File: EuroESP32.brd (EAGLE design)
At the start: 50.8 x 86.4 mm, 127 parts, among them IC1 TL074D, IC10 MCP6004, IC2 TL072, IC3 TL072, IC4 WM8731, IC5 TL074D, IC7 ADP7118, P4 POWER_SIMPLE10, U1 LM4040SOT23, U2 MCP3204-CI/SL

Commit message: A few corrections
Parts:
- moved REGULATOR 45.8 mm to (-5.08, -22.9)
- moved U$1 45.8 mm to (11.7, -10.4)
- moved U$2 45.8 mm to (11.7, -18.0)
- moved C1 45.8 mm to (-7.62, -33.0)
- moved C6 45.8 mm to (-2.54, -33.0)
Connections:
- removed net LHPOUT: IC4.9
- removed net MICBIAS: IC4.17
- removed net MICIN: IC4.18
- removed net RHPOUT: IC4.10

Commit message: Added groups in schematic
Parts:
- removed C15, C23, C25: 10uF, parts_aman:R0805
- removed C16, C27, C29, C46: 100nF, parts_aman:RESISTOR_0603
- removed C43, C45: 1uF, parts_aman:RESISTOR_0603
- removed REGULATOR: 7805TV, linear:TO220V
- added IC6: 7805T, adafruit:TO220H
- C1, C6: device TOF:C2.5-2 -> parts_aman:R1210
- moved C6 54.5 mm to (-50.8, -58.4), turned to 0 degrees
- moved C1 46.7 mm to (-50.8, -50.8)
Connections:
- net +12V: now also IC6.1; no longer REGULATOR.1
- net +3.3VA: no longer C15.1, C16.1, C23.2, C25.2, C27.2, C29.2, C43.2, C45.2, C46.2
- net 5V: now also IC6.3; no longer REGULATOR.3
- net GND: now also IC6.2; no longer C15.2, C16.2, C23.1, C25.1, C27.1, C29.1, C43.1, C45.1, C46.1, REGULATOR.2

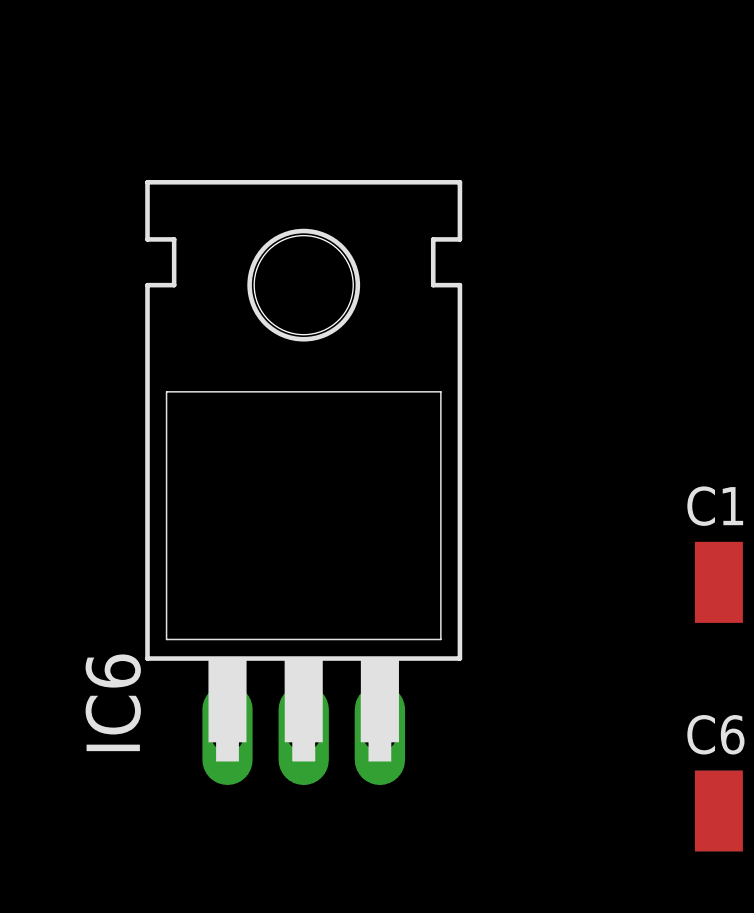
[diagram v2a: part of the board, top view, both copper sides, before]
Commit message: Changed voltage regulator
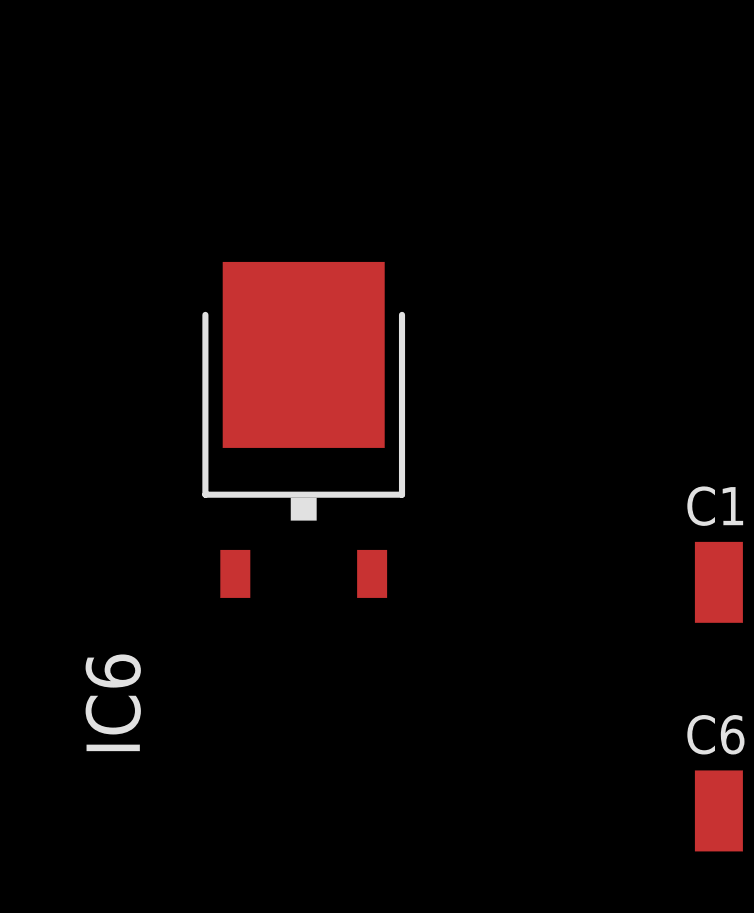
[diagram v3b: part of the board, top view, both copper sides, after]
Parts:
- IC6: value 7805T -> 7805DT; device adafruit:TO220H -> adafruit:TO252
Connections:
- net 5V: now also IC6.2; no longer IC6.3
- net GND: now also IC6.3; no longer IC6.2
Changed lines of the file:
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@@
 <attribute name="NAME" x="-53.34" y="-56.515" size="1.27" layer="25"/>
 </element>
-<element name="IC6" library="adafruit" package="TO220H" value="7805T" x="-66.04" y="-45.72" smashed="yes">
+<element name="IC6" library="adafruit" package="TO252" value="7805DT" x="-66.04" y="-45.72" smashed="yes">
 <attribute name="NAME" x="-71.501" y="-56.642" size="1.778" layer="25" ratio="10" rot="R90"/>
 <attribute name="VALUE" x="-58.674" y="-56.769" size="1.778" layer="27" ratio="10" rot="R90"/>
@@
 <contactref element="C1" pad="2"/>
 <contactref element="C6" pad="2"/>
-<contactref element="IC6" pad="2"/>
+<contactref element="IC6" pad="3"/>
 <wire x1="77.15" y1="97.79" x2="77.05" y2="99.695" width="0" layer="19" extent="16-16"/>
 <wire x1="72.3322" y1="99.65" x2="77.05" y2="99.695" width="0" layer="19" extent="16-16"/>
@@
 <wire x1="-49.4" y1="-50.8" x2="13.789" y2="-19.009" width="0" layer="19" extent="1-1"/>
 <wire x1="-49.4" y1="-58.42" x2="-49.4" y2="-50.8" width="0" layer="19" extent="1-1"/>
-<wire x1="-66.04" y1="-55.88" x2="-49.4" y2="-58.42" width="0" layer="19" extent="1-1"/>
+<wire x1="-66.04" y1="-43.22" x2="-49.4" y2="-50.8" width="0" layer="19" extent="1-1"/>
 </signal>
 <signal name="ADC_CS">
@@
 <wire x1="2.54" y1="45.72" x2="59.055" y2="47.473" width="0" layer="19" extent="16-16"/>
 <wire x1="-52.2" y1="-50.8" x2="2.54" y2="45.72" width="0" layer="19" extent="1-1"/>
-<wire x1="-68.58" y1="-55.88" x2="-52.2" y2="-50.8" width="0" layer="19" extent="1-1"/>
+<wire x1="-68.32" y1="-50.52" x2="-52.2" y2="-50.8" width="0" layer="19" extent="1-1"/>
 </signal>
 <signal name="-12V">
@@
 <contactref element="IC7" pad="3"/>
 <contactref element="C6" pad="1"/>
-<contactref element="IC6" pad="3"/>
-<wire x1="-52.2" y1="-58.42" x2="-63.5" y2="-55.88" width="0" layer="19" extent="1-1"/>
-<wire x1="-55.052" y1="36.546" x2="-63.5" y2="-55.88" width="0" layer="19" extent="1-1"/>
+<contactref element="IC6" pad="2"/>
+<wire x1="-52.2" y1="-58.42" x2="-63.76" y2="-50.52" width="0" layer="19" extent="1-1"/>
+<wire x1="-55.052" y1="36.546" x2="-63.76" y2="-50.52" width="0" layer="19" extent="1-1"/>
 <wire x1="-53.152" y1="36.546" x2="-55.052" y2="36.546" width="0" layer="19" extent="1-1"/>
 <wire x1="-53.978" y1="42.418" x2="-53.152" y2="36.546" width="0" layer="19" extent="1-1"/>

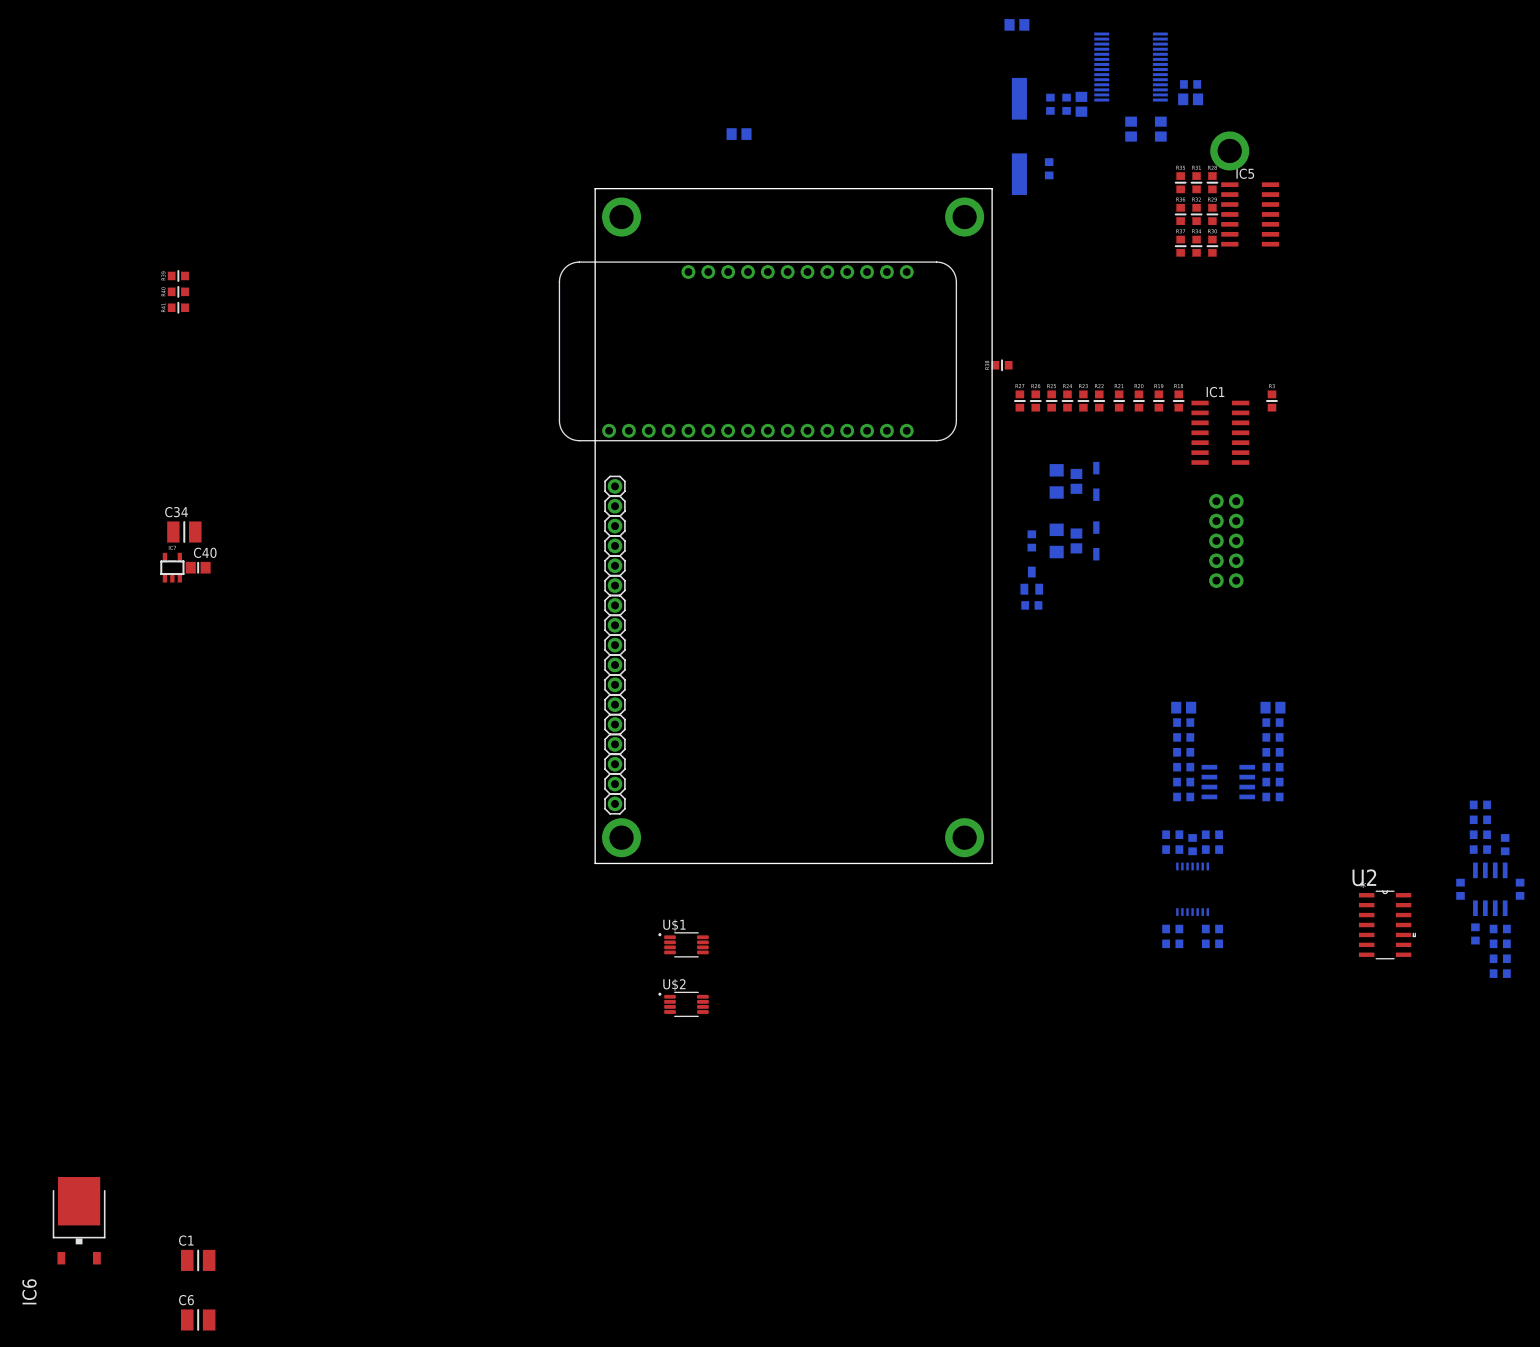
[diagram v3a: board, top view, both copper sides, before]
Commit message: Added groups and merged changes from alx-1
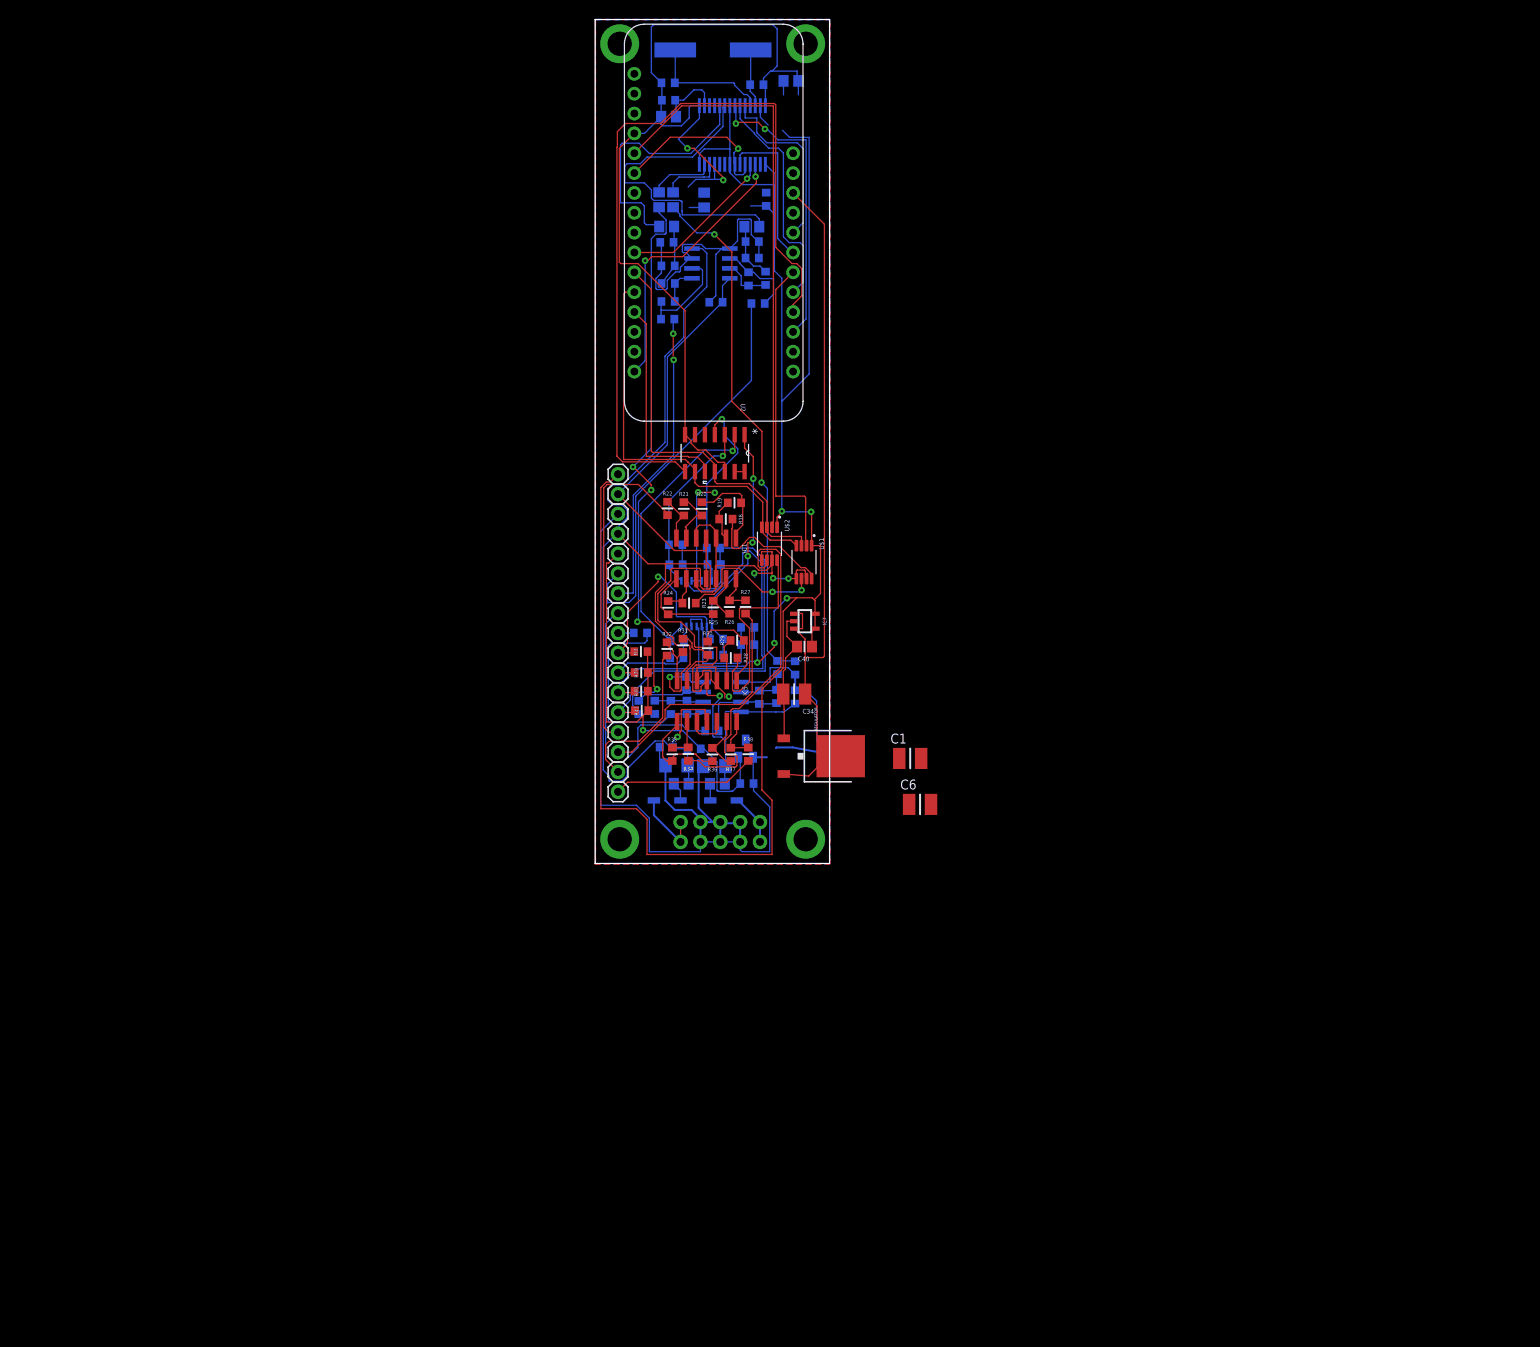
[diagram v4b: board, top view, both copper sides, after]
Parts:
- removed C30: 100nF, parts_aman:RESISTOR_0603
- removed C32: 10uF, parts_aman:R0805
- removed H2: PCB_SCREW, parts_aman:PCB_SCREW
- removed IC6: 7805DT, adafruit:TO252
- added C16: 100nF, parts_aman:RESISTOR_0603
- added C43: 1uF, parts_aman:RESISTOR_0603
- added REGULATOR: 7805DT, linear:TO252
- -10VREF: value -10VREF -> -10V
- CVIN(100K)0: value CVIN(100k)0 -> CVI0
- CVIN(100K)1: value CVIN(100K)1 -> CVI1
- CVIN(100K)2: value CVIN(100K)2 -> CVI2
- CVIN(100K)3: value CVIN(100K)3 -> CVI3
- CVOUT1: value CVOUT1 -> CVO1
- CVOUT2: value CVOUT2 -> CVO2
- CVOUT3: value CVOUT3 -> CVO3
- CVOUT4: value CVOUT4 -> CVO4
- moved C6 113.5 mm to (41.6, 7.56)
- moved C1 111.5 mm to (40.3, 13.4)
- moved R12 110.0 mm to (5.79, 29.5), turned to 0 degrees
- moved R1 108.4 mm to (5.58, 20.0), turned to 90 degrees
- moved C20 106.8 mm to (11.7, 23.0), turned to 270 degrees
- moved R6 106.6 mm to (7.63, 20.0), turned to 90 degrees
- moved R13 105.4 mm to (14.9, 17.0), turned to 0 degrees
- moved U2 104.9 mm to (15.3, 52.5), turned to 270 degrees
- moved C7 104.9 mm to (9.69, 20.0), turned to 90 degrees
- moved R10 103.2 mm to (11.7, 20.0), turned to 270 degrees
- moved H3 101.6 mm to (3.14, 104.9), turned to 270 degrees
- moved IC3 101.3 mm to (16.2, 21.3), turned to 90 degrees
- moved R7 99.7 mm to (23.3, 25.1), turned to 270 degrees
- moved R11 99.3 mm to (21.0, 21.3), turned to 270 degrees
- moved C12 99.1 mm to (9.15, 81.5), turned to 180 degrees
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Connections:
- net +12V: now also REGULATOR.1; no longer IC6.1
- net +3.3VA: now also C16.1, C43.2; no longer C30.2, C32.1
- net 5V: now also REGULATOR.2; no longer IC6.2
- net GND: now also C16.2, C43.1, REGULATOR.3; no longer C30.1, C32.2, IC6.3
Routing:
- net GND: track 0.00 -> 439.4 mm, vias 0 -> 8
- net +3.3VA: track 0.00 -> 277.6 mm, vias 0 -> 5
- net -12V: track 0.00 -> 149.2 mm, vias 0 -> 2
- net +12V: track 0.00 -> 120.7 mm, vias 0 -> 1
- net ADC_CS: track 0.00 -> 101.6 mm
- net 5V: track 0.00 -> 91.1 mm
- net N$49: track 0.00 -> 76.5 mm, vias 0 -> 4
- net DAC34_CS: track 0.00 -> 74.3 mm
- net N$57: track 0.00 -> 67.2 mm, vias 0 -> 2
- net -10VREF: track 0.00 -> 59.4 mm, vias 0 -> 1
- net N$15: track 0.00 -> 54.7 mm
- net SPI_MOSI: track 0.00 -> 52.8 mm
- net SPI_CLK: track 0.00 -> 52.3 mm
- net N$21: track 0.00 -> 51.9 mm
- net N$1: track 0.00 -> 51.8 mm
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- added copper zone on layer 1, net GND
- added copper zone on layer 16, net GND
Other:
- board size 50.8 x 86.4 mm -> 30 x 108 mm

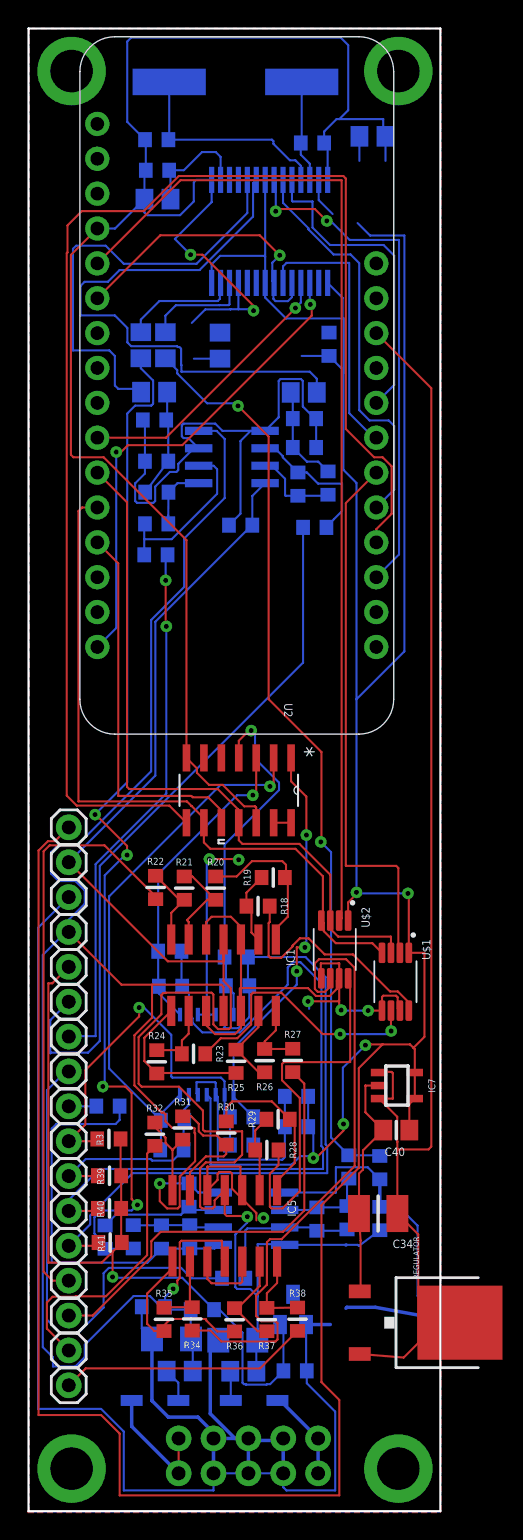
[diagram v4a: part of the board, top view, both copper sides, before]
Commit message: Moved connecters to the side
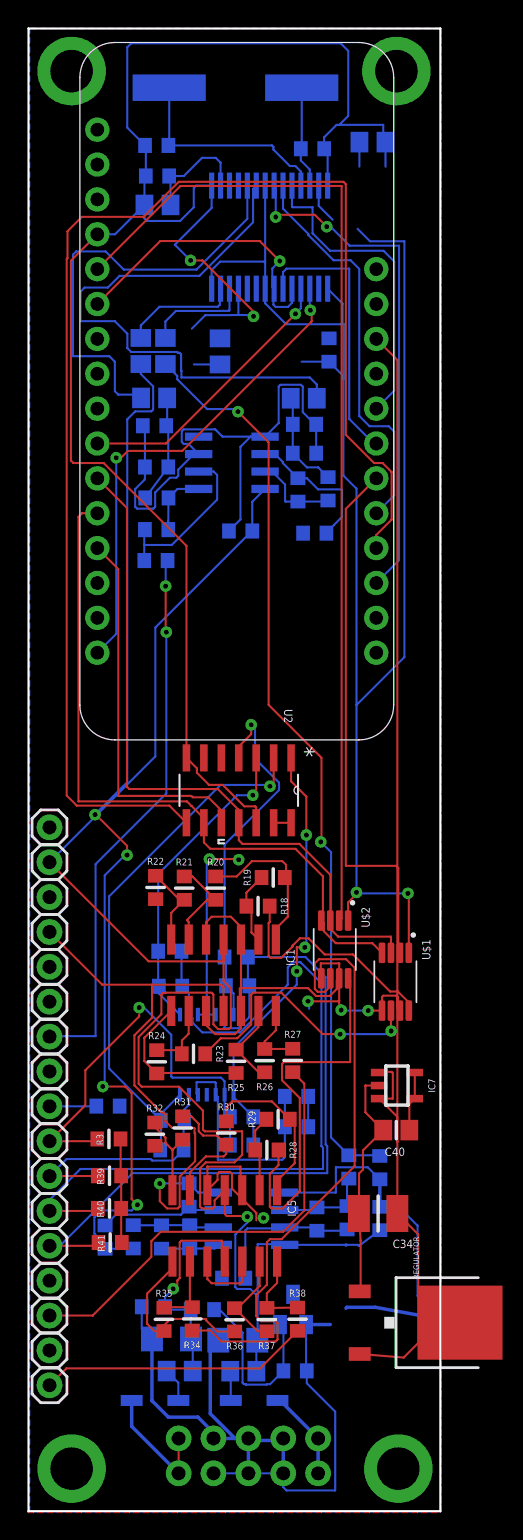
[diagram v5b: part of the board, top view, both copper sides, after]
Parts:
- moved +12V 1.40 mm to (1.53, 47.3), turned to 180 degrees
- moved +3.3VA 1.40 mm to (1.53, 49.8), turned to 180 degrees
- moved -10VREF 1.40 mm to (1.53, 39.6), turned to 180 degrees
- moved -12V 1.40 mm to (1.53, 42.2), turned to 180 degrees
- moved CVIN(100K)0 1.40 mm to (1.53, 26.9), turned to 180 degrees
- moved CVIN(100K)1 1.40 mm to (1.53, 24.4), turned to 180 degrees
- moved CVIN(100K)2 1.40 mm to (1.53, 21.9), turned to 180 degrees
- moved CVIN(100K)3 1.40 mm to (1.53, 19.3), turned to 180 degrees
- moved CVOUT1 1.40 mm to (1.53, 16.8), turned to 180 degrees
- moved CVOUT2 1.40 mm to (1.53, 14.2), turned to 180 degrees
- moved CVOUT3 1.40 mm to (1.53, 11.7), turned to 180 degrees
- moved CVOUT4 1.40 mm to (1.53, 9.17), turned to 180 degrees
- moved GND 1.40 mm to (1.53, 44.7), turned to 180 degrees
- moved J_LIN 1.40 mm to (1.53, 37.1), turned to 180 degrees
- moved J_LOUT 1.40 mm to (1.53, 32.0), turned to 180 degrees
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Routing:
- net +3.3VA: track 277.6 -> 131.6 mm, vias 5 -> 2
- net -12V: track 149.2 -> 60.2 mm
- net GND: track 439.4 -> 378.9 mm
- net N$1: track 51.8 -> 0.00 mm
- net N$25: track 42.8 -> 0.00 mm
- net -10VREF: track 59.4 -> 20.9 mm, vias 1 -> 0
- net N$2: track 35.8 -> 0.00 mm
- net N$46: track 28.7 -> 4.25 mm
- net N$29: track 21.1 -> 0.00 mm
- net 5V: track 91.1 -> 86.7 mm
- net N$15: track 54.7 -> 57.5 mm
- net N$19: track 15.6 -> 18.4 mm
- net N$21: track 51.9 -> 54.3 mm
- net N$17: track 29.0 -> 31.0 mm
- net +12V: track 120.7 -> 122.2 mm
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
